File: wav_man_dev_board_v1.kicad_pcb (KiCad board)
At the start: 2 copper layers, 80 x 100 mm, 97 parts, among them J1 Micro_SD_Card, J3 AudioJack3, J4 BATTERY, P1 USB_C_Plug_USB2.0, Q1 MMBT2222A, Q2 MMBT2222A, Q3 MMBT2222A, Q4 MMBT2222A, SW1 PAGE_M, SW10 DISP_VIEW, SW11 STOP, SW12 ALPHA, SW14 HOLD, SW15 MCU_RESET, SW16 PWR_SW, SW2 PAGE_P, SW3 TAB_M, SW4 TAB_P, SW5 PLAY_PAUSE, SW6 TRACK_FF, SW7 TRACK_RW, SW8 TRACK_RPT, SW9 PLYLST_RNDM, U1 PCM5102A, U2 AZ1117-3.3, U3 ATSAMD21G18A-A, U4 LM4810

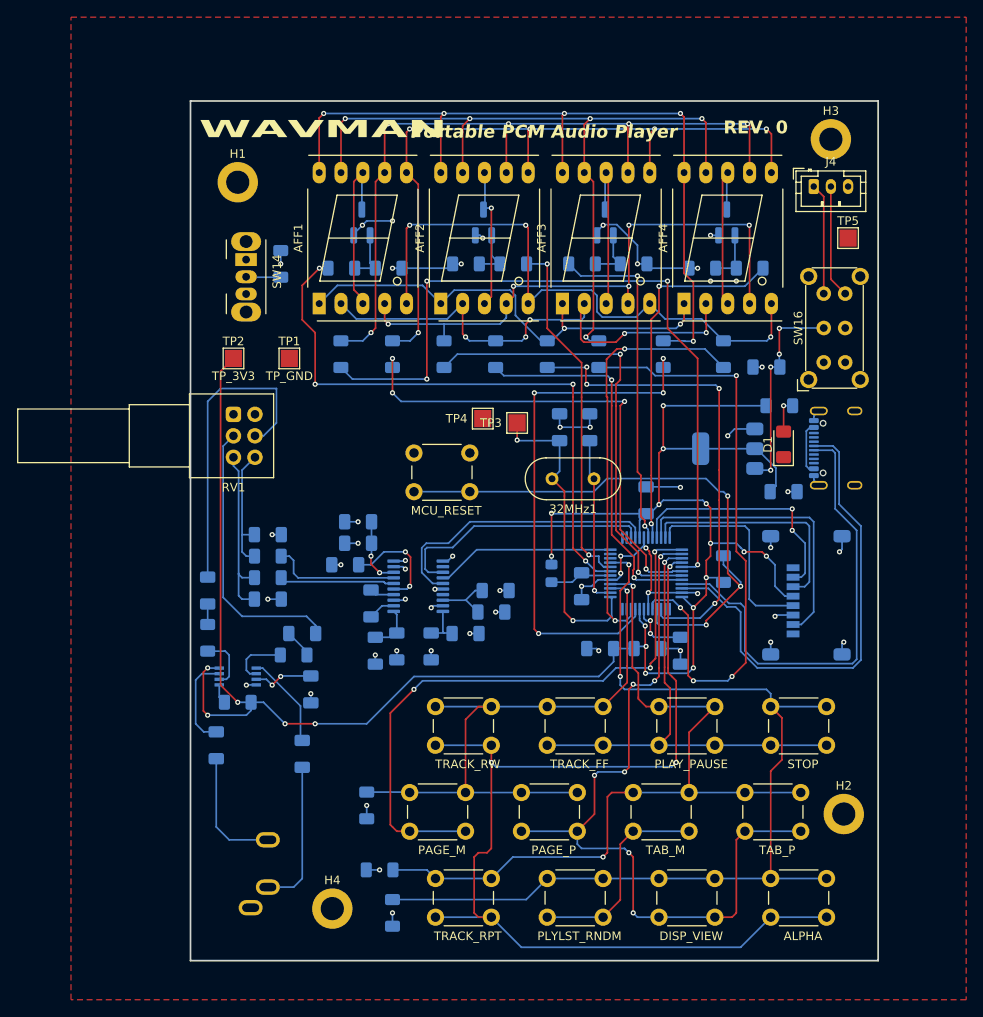
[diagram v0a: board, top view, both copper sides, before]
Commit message: usb fixed, rerouted some traces
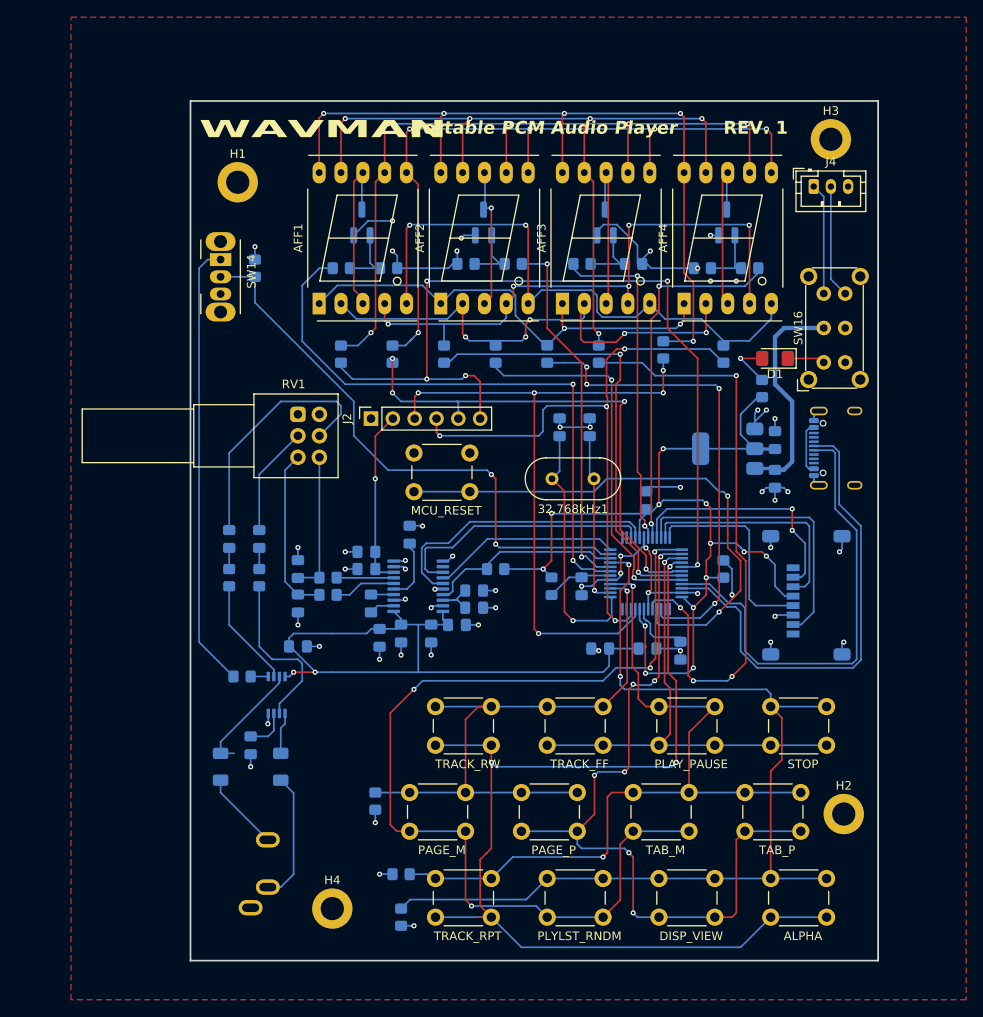
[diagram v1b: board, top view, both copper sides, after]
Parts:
- removed TP1, TP4, TP5: TP_GND, TestPoint:TestPoint_Pad_2.0x2.0mm
- removed TP2: TP_3V3, TestPoint:TestPoint_Pad_2.0x2.0mm
- removed TP3: TP_CLK, TestPoint:TestPoint_Pad_2.0x2.0mm
- added C27: 1uF, Capacitor_SMD:C_0805_2012Metric_Pad1.18x1.45mm_HandSolder, B.Cu at (128.0, 124.0)
- added J2: DEBUG, Connector_PinSocket_2.54mm:PinSocket_1x06_P2.54mm_Vertical, F.Cu at (136.5, 97.5)
- added R18: 10k, Resistor_SMD:R_0805_2012Metric_Pad1.20x1.40mm_HandSolder, B.Cu at (151.0, 115.0)
- C1, C10, C11, C12, C13, C16, C17, C18, C19, C2, C20, C21, C22, C23, C24, C25, C26, C3, C4, C5, C6, C7, C8, C9: footprint Capacitor_SMD:C_1206_3216Metric_Pad1.33x1.80mm_HandSolder -> Capacitor_SMD:C_0805_2012Metric_Pad1.18x1.45mm_HandSolder
- R1, R11, R12, R13, R14, R15, R16, R17, R2, R3, R32, R33, R34, R35, R36, R37, R38, R39, R4, R40, R41, R5, R6, R7, R8: footprint Resistor_SMD:R_1206_3216Metric_Pad1.30x1.75mm_HandSolder -> Resistor_SMD:R_0805_2012Metric_Pad1.20x1.40mm_HandSolder
- R10, R9: value ? -> 100; footprint Resistor_SMD:R_1206_3216Metric_Pad1.30x1.75mm_HandSolder -> Resistor_SMD:R_0805_2012Metric_Pad1.20x1.40mm_HandSolder
- moved C22 13.0 mm to (183.5, 104.5), turned to -90 degrees
- moved C16 12.1 mm to (123.5, 111.5), turned to -90 degrees
- moved D1 10.0 mm to (183.5, 90.5), turned to 180 degrees
- moved R34 9.85 mm to (123.5, 116.0), turned to -90 degrees
- moved C18 9.55 mm to (122.5, 135.5)
- moved C12 8.28 mm to (141.0, 111.0), turned to 90 degrees
- moved RV1 7.50 mm to (128.0, 97.0)
- moved R33 7.43 mm to (131.5, 116.0)
- moved R35 7.43 mm to (120.0, 116.0)
- moved R32 7.28 mm to (131.5, 118.0)
- moved C17 6.50 mm to (120.0, 111.5)
- moved C24 6.08 mm to (183.5, 100.0), turned to 90 degrees
- moved C2 5.32 mm to (128.0, 115.0), turned to -90 degrees
- moved U4 5.01 mm to (125.5, 129.7), turned to 90 degrees
- moved C5 3.63 mm to (136.0, 113.0)
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- renumbered 32MHz1 to 32.768kHz1
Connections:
- C10 pad 1: Net-(U1-CPVDD) -> 3.3V
- C11 pad 1: Net-(U1-CPVDD) -> 3.3V
- C4 pad 1: Net-(U1-AVDD) -> 3.3V
- C5 pad 1: Net-(U1-AVDD) -> 3.3V
- C8 pad 1: Net-(U1-DVDD) -> 3.3V
- C9 pad 1: Net-(U1-DVDD) -> 3.3V
- P1 pad A8: (no net) -> unconnected-(P1-SBU1-PadA8)
- P1 pad B6: (no net) -> USB_DP
- P1 pad B7: (no net) -> USB_DM
- P1 pad B8: (no net) -> unconnected-(P1-SBU2-PadB8)
- SW14 pad 1: 3V -> 3.3V
- SW3 pad 2: Net-(SW3-Pad2) -> SW_COL_A
- SW9 pad 2: Net-(SW3-Pad2) -> SW_COL_A
- U1 pad 1: Net-(U1-CPVDD) -> 3.3V
- U1 pad 20: Net-(U1-DVDD) -> 3.3V
- U1 pad 8: Net-(U1-AVDD) -> 3.3V
- U3 pad 10: unconnected-(U3-PA05-Pad10) -> PCM_MUTE
- U3 pad 11: unconnected-(U3-PA06-Pad11) -> HOLD
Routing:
- net HOLD: track 4.05 -> 67.2 mm, vias 0 -> 2
- net SW_COL_A: track 71.6 -> 114.4 mm, vias 3 -> 4
- net 3.3V: track 228.3 -> 263.8 mm, vias 20 -> 16
- net Net-(SW3-Pad2): track 24.4 -> 0.00 mm
- net DISP_SEG_DOT: track 48.7 -> 73.0 mm, vias 2 -> 4
- net PCM_MUTE: track 0.00 -> 22.8 mm
- net Net-(C16-Pad1): track 32.3 -> 12.8 mm
- net VBAT-: track 125.2 -> 143.7 mm, vias 53 -> 55
- net DISP_SEG_G: track 61.2 -> 76.8 mm, vias 4 -> 5
- net Net-(U4-VIN1): track 6.75 -> 19.7 mm
- net DISP_SEG_A: track 86.3 -> 97.3 mm, vias 4 -> 5
- net Net-(U1-OUTR): track 15.0 -> 6.65 mm
- net Net-(U1-AVDD): track 8.02 -> 0.00 mm, vias 2 -> 0
- net Net-(C17-Pad1): track 36.2 -> 29.2 mm
- net MCU_XIN: track 36.3 -> 29.3 mm, vias 2 -> 1
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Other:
- board text added: "REV. 1"
- board text removed: "REV. 0"

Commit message: minor silkscreen and trace mods
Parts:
- renumbered 32.768kHz1 to 32.768kHz
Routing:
- net USB_DM: track 55.0 -> 60.3 mm, vias 0 -> 2
- net USB_DP: track 56.2 -> 61.3 mm, vias 0 -> 2
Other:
- board text added: "HOLD"
- board text added: "MICRO SD"
- board text added: "PHONES"
- board text added: "PWR"
- board text added: "REV 1"
- board text added: "USB"
- board text added: "VOL"
- board text removed: "REV. 1"
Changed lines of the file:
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@@
 		(property "Value" "TRACK_RW"
 			(at 3.75 6.7 0)
-			(layer "F.SilkS")
+			(layer "F.SilkS" knockout)
 			(effects
 				(font
@@
 		(at 162.44 104.5 180)
 		(descr "HC-49/U, Crystal, http://5hertz.com/pdfs/04404_D.pdf")
-		(property "Reference" "32.768kHz1"
+		(property "Reference" "32.768kHz"
 			(at 2.44 -3.52 0)
 			(layer "F.SilkS")
@@
 		(property "Value" "DISP_VIEW"
 			(at 3.75 6.7 0)
-			(layer "F.SilkS")
+			(layer "F.SilkS" knockout)
 			(effects
 				(font
@@
 		(property "Value" "TAB_M"
 			(at 3.75 6.7 0)
-			(layer "F.SilkS")
+			(layer "F.SilkS" knockout)
 			(effects
 				(font
@@
 		(property "Value" "TRACK_FF"
 			(at 3.75 6.7 0)
-			(layer "F.SilkS")
+			(layer "F.SilkS" knockout)
 			(effects
 				(font
@@
 		(property "Value" "PLYLST_RNDM"
 			(at 3.75 6.7 0)
-			(layer "F.SilkS")
+			(layer "F.SilkS" knockout)
 			(effects
 				(font
@@
 		(property "Value" "PAGE_P"
 			(at 3.75 6.7 0)
-			(layer "F.SilkS")
+			(layer "F.SilkS" knockout)
 			(effects
 				(font
@@
 		(property "Value" "STOP"
 			(at 3.75 6.7 0)
-			(layer "F.SilkS")
+			(layer "F.SilkS" knockout)
 			(effects
 				(font
@@
 		(property "Value" "PLAY_PAUSE"
 			(at 3.75 6.7 0)
-			(layer "F.SilkS")
+			(layer "F.SilkS" knockout)
 			(effects
 				(font
@@
 		(property "Value" "PAGE_M"
 			(at 3.75 6.7 0)
-			(layer "F.SilkS")
+			(layer "F.SilkS" knockout)
 			(effects
 				(font
@@
 	)
 	(footprint "Button_Switch_THT:SW_E-Switch_EG2219_DPDT_Angled"
+		(locked yes)
 		(layer "F.Cu")
 		(at 189.1675 90.9575 90)
@@
 		(property "Value" "MCU_RESET"
 			(at 3.75 6.7 0)
-			(layer "F.SilkS")
+			(layer "F.SilkS" knockout)
 			(effects
 				(font
@@
 		(property "Value" "ALPHA"
 			(at 3.75 6.7 0)
-			(layer "F.SilkS")
+			(layer "F.SilkS" knockout)
 			(effects
 				(font
@@
 		(property "Value" "TRACK_RPT"
 			(at 3.75 6.7 0)
-			(layer "F.SilkS")
+			(layer "F.SilkS" knockout)
 			(effects
 				(font
@@
 		(property "Value" "TAB_P"
 			(at 3.75 6.7 0)
-			(layer "F.SilkS")
+			(layer "F.SilkS" knockout)
 			(effects
 				(font
@@
 		)
 	)
-	(gr_text "REV. 1"
+	(gr_text "REV 1"
 		(locked yes)
 		(at 177.5 64.5435 0)
@@
 		)
 	)
+	(gr_text "VOL"
+		(at 118 105.5 0)
+		(layer "F.SilkS" knockout)
+		(effects
+			(font
+				(size 1 1)
+				(thickness 0.15)
+			)
+		)
+	)
+	(gr_text "HOLD"
+		(at 118.5 88 0)
+		(layer "F.SilkS" knockout)
+		(effects
+			(font
+				(size 1 1)
+				(thickness 0.15)
+			)
+		)
+	)
+	(gr_text "PWR"
+		(at 192.5 78.5 0)
+		(layer "F.SilkS" knockout)
+		(effects
+			(font
+				(size 1 1)
+				(thickness 0.15)
+			)
+		)
+	)
+	(gr_text "USB"
+		(at 192.5 107.5 -0)
+		(layer "B.SilkS" knockout)
+		(effects
+			(font
+				(size 1 1)
+				(thickness 0.15)
+			)
+			(justify mirror)
+		)
+	)
+	(gr_text "MICRO SD"
+		(at 190.5 127 -0)
+		(layer "B.SilkS" knockout)
+		(effects
+			(font
+				(size 1 1)
+				(thickness 0.15)
+			)
+			(justify mirror)
+		)
+	)
+	(gr_text "PHONES"
+		(at 117 154 -90)
+		(layer "B.SilkS" knockout)
+		(effects
+			(font
+				(size 1 1)
+				(thickness 0.15)
+			)
+			(justify mirror)
+		)
+	)
 	(segment
 		(start 162.44 117.44)
@@
 	)
 	(segment
+		(start 190 100)
+		(end 190.5 100.5)
+		(width 0.2)
+		(layer "F.Cu")
+		(net 40)
+	)
+	(segment
+		(start 190.5 100.780033)
+		(end 189.576381 101.703652)
+		(width 0.2)
+		(layer "F.Cu")
+		(net 40)
+	)
+	(segment
+		(start 190.5 100.5)
+		(end 190.5 100.780033)
+		(width 0.2)
+		(layer "F.Cu")
+		(net 40)
+	)
+	(via
+		(at 189.576381 101.703652)
+		(size 0.6)
+		(drill 0.3)
+		(layers "F.Cu" "B.Cu")
+		(net 40)
+	)
+	(via
+		(at 190 100)
+		(size 0.6)
+		(drill 0.3)
+		(layers "F.Cu" "B.Cu")
+		(net 40)
+	)
+	(segment
+		(start 189.5 100)
+		(end 190 100)
+		(width 0.2)
+		(layer "B.Cu")
+		(net 40)
+	)
+	(segment
+		(start 189.32 100.18)
+		(end 189.5 100)
+		(width 0.2)
+		(layer "B.Cu")
+		(net 40)
+	)
+	(segment
 		(start 181.5 126)
 		(end 192.5 126)
@@
 	)
 	(segment
+		(start 188.02 100.18)
+		(end 189.32 100.18)
+		(width 0.2)
+		(layer "B.Cu")
+		(net 40)
+	)
+	(segment
 		(start 180 119.5)
 		(end 180 124.5)
@@
 	)
 	(segment
+		(start 190.5 102)
+		(end 189.872729 102)
+		(width 0.2)
+		(layer "B.Cu")
+		(net 40)
+	)
+	(segment
 		(start 192.5 126)
 		(end 193 125.5)
@@
 	(segment
 		(start 190.5 108)
-		(end 190.5 101.5)
+		(end 190.5 102)
+		(width 0.2)
+		(layer "B.Cu")
+		(net 40)
+	)
+	(segment
+		(start 189.872729 102)
+		(end 189.576381 101.703652)
 		(width 0.2)
 		(layer "B.Cu")
@@
 	)
 	(segment
+		(start 190.5 102)
+		(end 190.5 101.5)
+		(width 0.2)
+		(layer "B.Cu")
+		(net 40)
+	)
+	(segment
 		(start 172.6625 116.75)
 		(end 175.88884 116.75)
@@
 	)
 	(segment
+		(start 189.5 102.5)
+		(end 191.5 102.5)
+		(width 0.2)
+		(layer "F.Cu")
+		(net 41)
+	)
+	(via
+		(at 191.5 102.5)
+		(size 0.6)
+		(drill 0.3)
+		(layers "F.Cu" "B.Cu")
+		(net 41)
+	)
+	(via
+		(at 189.5 102.5)
+		(size 0.6)
+		(drill 0.3)
+		(layers "F.Cu" "B.Cu")
+		(net 41)
+	)
+	(segment
 		(start 193.5 110)
 		(end 193.5 125.5671)
@@
 	)
 	(segment
+		(start 188.68 101.68)
+		(end 189.5 102.5)
+		(width 0.2)
+		(layer "B.Cu")
+		(net 41)
+	)
+	(segment
 		(start 190.959 107.459)
 		(end 193.5 110)
@@
 	)
 	(segment
+		(start 191.5 101.9329)
+		(end 190.959 101.3919)
+		(width 0.2)
+		(layer "B.Cu")
+		(net 41)
+	)
+	(segment
 		(start 179.5 120)
 		(end 178.901 119.401)
@@
 	)
 	(segment
+		(start 188.02 101.68)
+		(end 188.68 101.68)
+		(width 0.2)
+		(layer "B.Cu")
+		(net 41)
+	)
+	(segment
+		(start 191.5 102.5)
+		(end 191.5 101.9329)
+		(width 0.2)
+		(layer "B.Cu")
+		(net 41)
+	)
+	(segment
 		(start 175.75 117.25)
 		(end 172.6625 117.25)
@@
 		(start 190 81.29)
 		(end 190 70.5)
-		(width 0.2)
+		(width 0.5)
 		(layer "B.Cu")
 		(net 87)
@@
 		(start 191.6675 82.9575)
 		(end 190 81.29)
-		(width 0.2)
+		(width 0.5)
 		(layer "B.Cu")
 		(net 87)
@@
 		(start 189.1675 71.6675)
 		(end 189.1675 82.9575)
-		(width 0.2)
+		(width 0.5)
 		(layer "B.Cu")
 		(net 88)
@@
 		(start 188 70.5)
 		(end 189.1675 71.6675)
-		(width 0.2)
+		(width 0.5)
 		(layer "B.Cu")
 		(net 88)

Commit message: minor fixes to audio amp, updated readme
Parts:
- added R19: 20k, Resistor_SMD:R_0805_2012Metric_Pad1.20x1.40mm_HandSolder, B.Cu at (129.0, 131.0)
- added R20: 20k, Resistor_SMD:R_0805_2012Metric_Pad1.20x1.40mm_HandSolder, B.Cu at (119.5, 131.0)
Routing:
- net 3.3V: track 263.8 -> 299.5 mm
- net Net-(U4-VIN2): track 12.7 -> 19.8 mm
- net Net-(U4-VOUT1): track 4.84 -> 7.76 mm
- net Net-(U4-VIN1): track 19.7 -> 21.5 mm
- net Net-(U4-VOUT2): track 13.3 -> 14.3 mm

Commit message: rev1 final commit
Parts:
- R12, R14: value ? -> 100
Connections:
- P1 pad A4: Net-(P1-VBUS-PadA4) -> unconnected-(P1-VBUS-PadA4)
- P1 pad A9: Net-(P1-VBUS-PadA4) -> unconnected-(P1-VBUS-PadA4)_3
- P1 pad B4: Net-(P1-VBUS-PadA4) -> unconnected-(P1-VBUS-PadA4)_1
- P1 pad B9: Net-(P1-VBUS-PadA4) -> unconnected-(P1-VBUS-PadA4)_2
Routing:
- net 3.3V: track 299.5 -> 326.7 mm, vias 16 -> 18
- net VBAT-: track 143.7 -> 150.2 mm, vias 55 -> 56
- net Net-(P1-VBUS-PadA4): track 6.13 -> 0.00 mm
- net SW_COL_D: track 124.2 -> 122.7 mm
- net DISP_SEG_E: track 55.6 -> 56.7 mm
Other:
- board text added: "3.3V"
- board text added: "CLK"
- board text added: "DIO"
- board text added: "GND"
- board text added: "RX"
- board text added: "TX"
